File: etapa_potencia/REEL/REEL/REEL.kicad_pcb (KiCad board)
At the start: 2 copper layers, 93.2 x 73.9 mm, 55 parts, among them J4 Conn_audio, J6 Salida_amp, U1 Tp5400, U2 ESP32-WROOM-32, U4 AMS1117-3.3

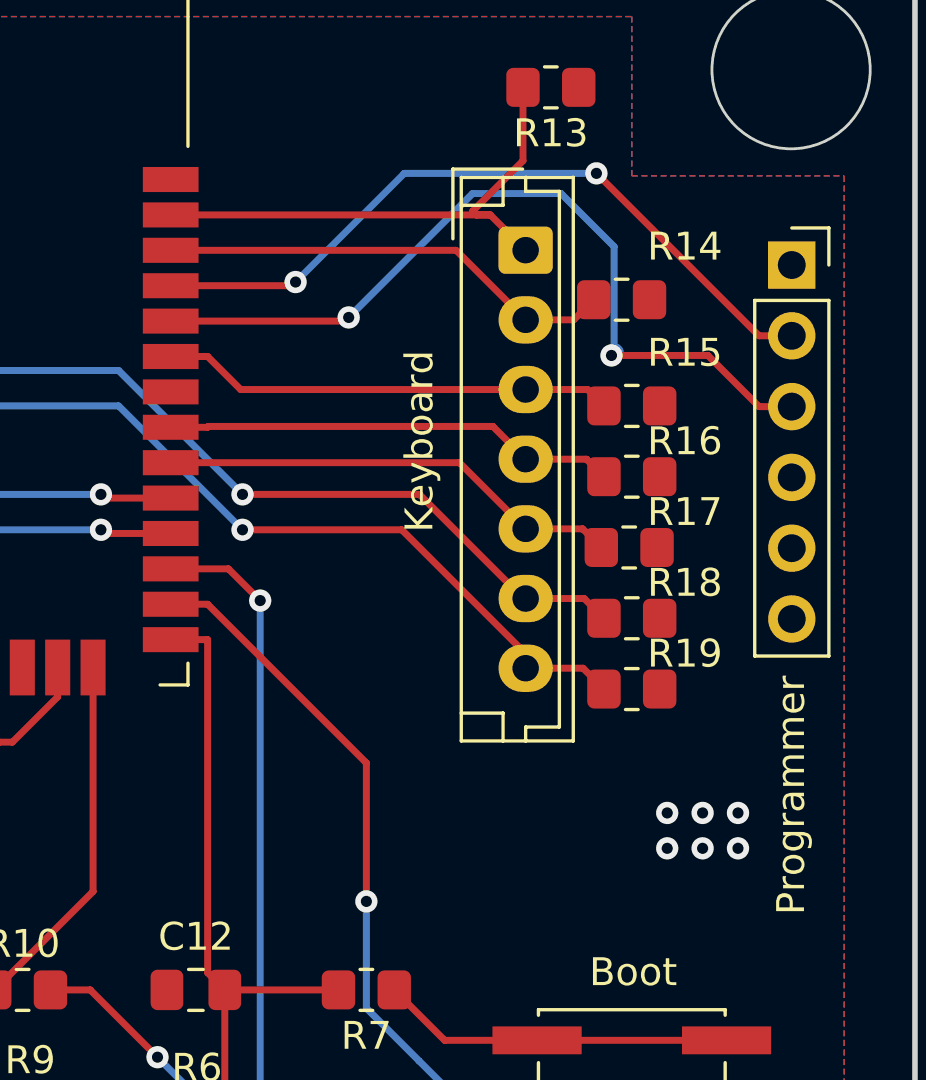
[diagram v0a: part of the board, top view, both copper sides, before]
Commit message: Corrección errores DCR
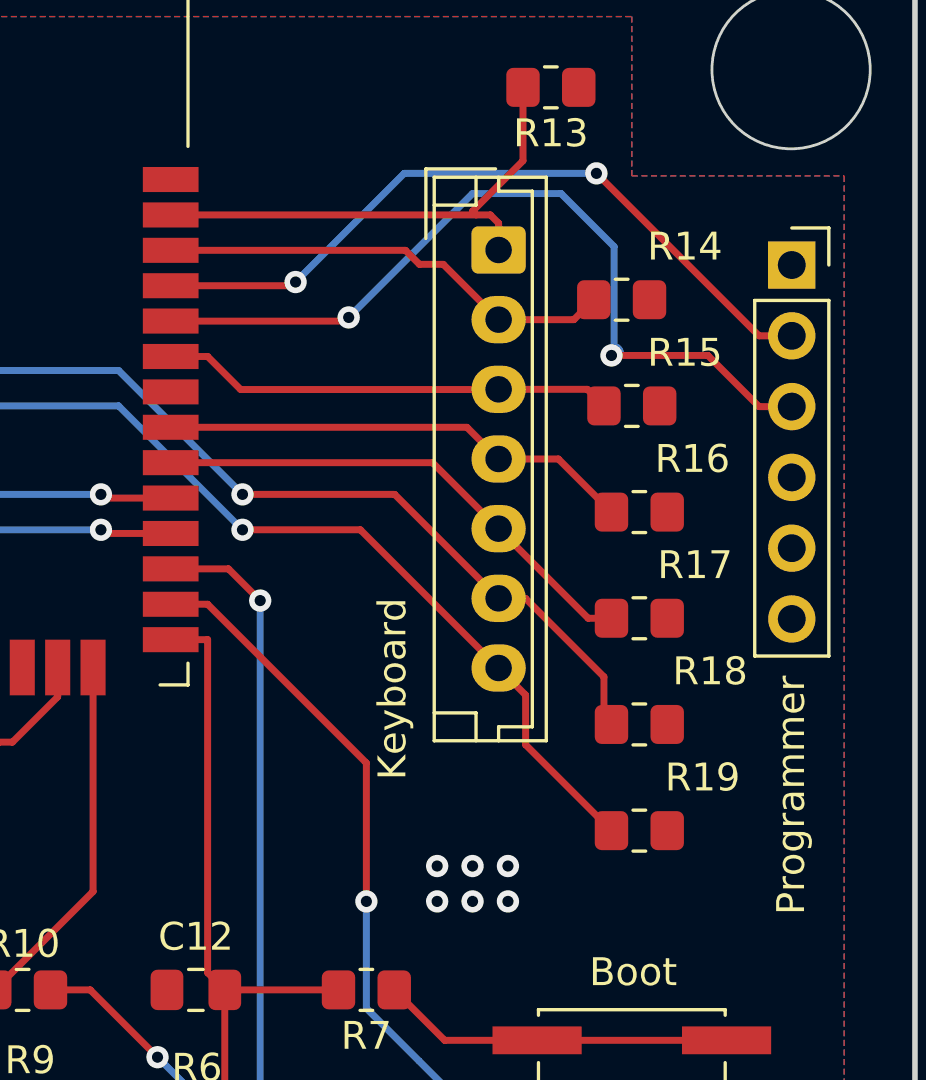
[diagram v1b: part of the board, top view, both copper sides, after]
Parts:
- moved R19 5.09 mm to (119.0, 87.6)
- moved R18 3.82 mm to (119.0, 83.8)
- moved R17 2.57 mm to (119.0, 80.0)
- moved R16 1.30 mm to (119.0, 76.2)
- moved Keyboard 0.97 mm to (114.0, 66.8)
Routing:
- net /T7: track 37.3 -> 40.4 mm
- net /T6: track 36.4 -> 39.0 mm
- net /T5: track 16.7 -> 18.1 mm
- net /T1: track 19.1 -> 18.2 mm
- net /T4: track 16.3 -> 17.1 mm

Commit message: Archivos gerber, drill, BOM y pos
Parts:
- moved C11 1.42 mm to (84.5, 100.1)
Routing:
- net Net-(C1-Pad1): track 64.4 -> 63.1 mm
- net /EN: track 53.9 -> 52.9 mm
